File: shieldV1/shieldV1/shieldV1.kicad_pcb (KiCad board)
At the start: 2 copper layers, 70 x 59 mm, 2 parts, among them J1 Conn_02x19_Odd_Even, J2 Conn_02x19_Odd_Even

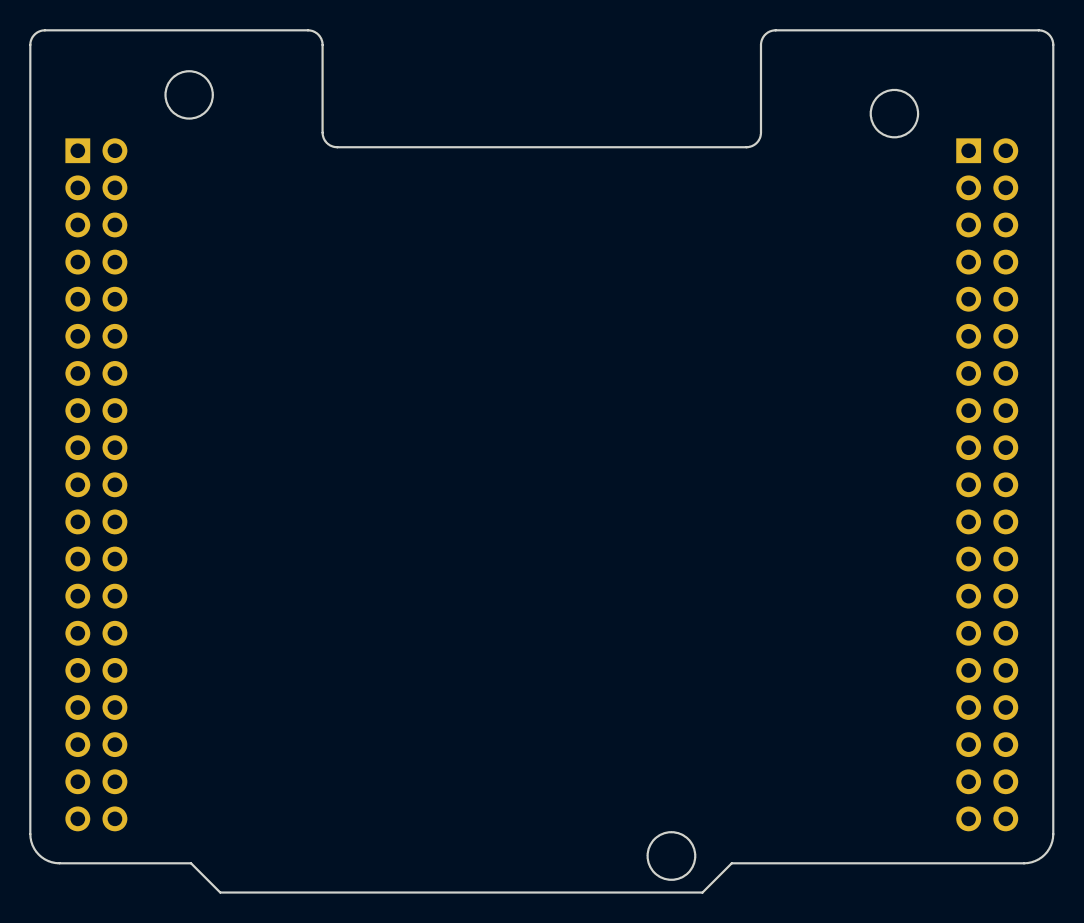
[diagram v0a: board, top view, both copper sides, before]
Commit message: Add hall sensor PCB
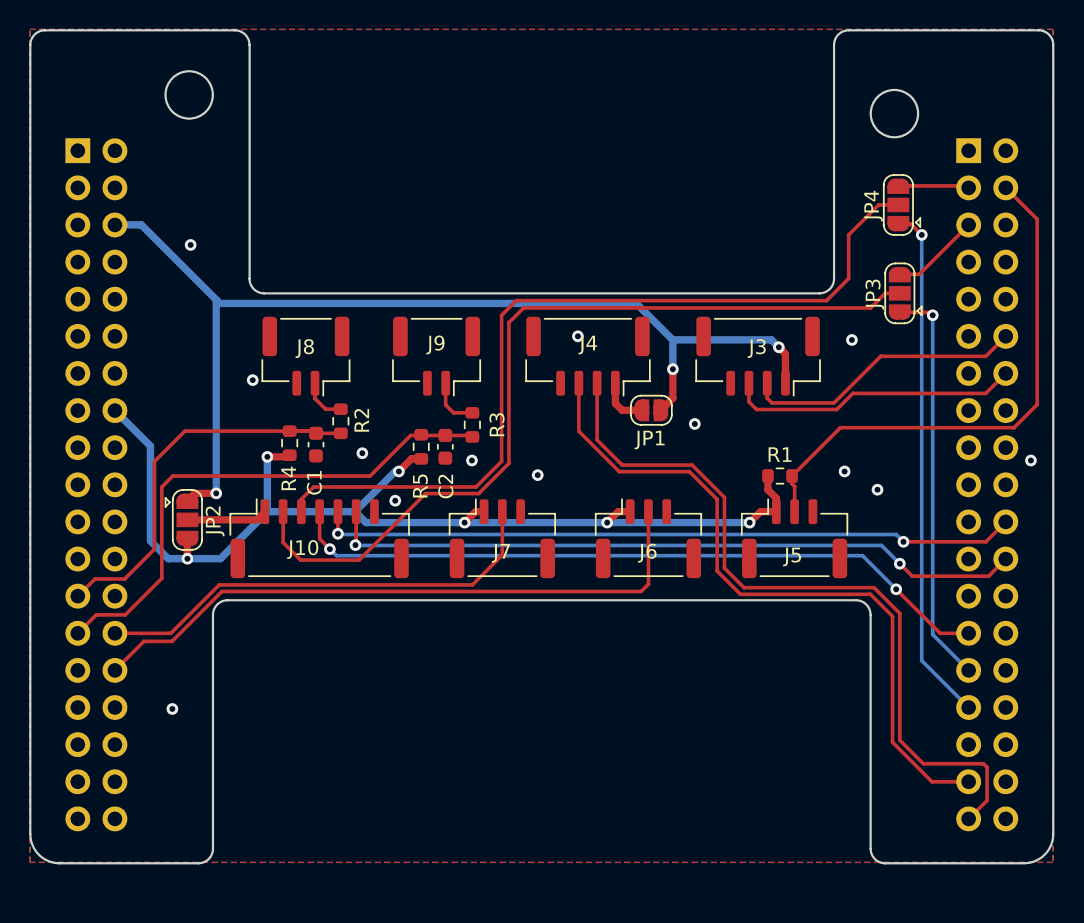
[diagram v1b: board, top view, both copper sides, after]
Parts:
- added C1: C, Capacitor_SMD:C_0603_1608Metric, F.Cu at (52.1, 121.7)
- added C2: C, Capacitor_SMD:C_0603_1608Metric, F.Cu at (60.9, 121.8)
- added J10: Conn_01x07_Female, Connector_JST:JST_GH_SM07B-GHS-TB_1x07-1MP_P1.25mm_Horizontal, F.Cu at (52.3, 128.1)
- added J3: Conn_01x04_Female, Connector_JST:JST_GH_SM04B-GHS-TB_1x04-1MP_P1.25mm_Horizontal, F.Cu at (82.3, 115.6)
- added J4: Conn_01x04_Female, Connector_JST:JST_GH_SM04B-GHS-TB_1x04-1MP_P1.25mm_Horizontal, F.Cu at (70.7, 115.6)
- added J5: Conn_01x03_Female, Connector_JST:JST_GH_SM03B-GHS-TB_1x03-1MP_P1.25mm_Horizontal, F.Cu at (84.8, 128.1)
- added J6: Conn_01x03_Female, Connector_JST:JST_GH_SM03B-GHS-TB_1x03-1MP_P1.25mm_Horizontal, F.Cu at (74.8, 128.1)
- added J7: Conn_01x03_Female, Connector_JST:JST_GH_SM03B-GHS-TB_1x03-1MP_P1.25mm_Horizontal, F.Cu at (64.8, 128.1)
- added J8: Conn_01x02_Female, Connector_JST:JST_GH_SM02B-GHS-TB_1x02-1MP_P1.25mm_Horizontal, F.Cu at (51.4, 115.6)
- added J9: Conn_01x02_Female, Connector_JST:JST_GH_SM02B-GHS-TB_1x02-1MP_P1.25mm_Horizontal, F.Cu at (60.3, 115.6)
- added JP1: SolderJumper_2_Open, Jumper:SolderJumper-2_P1.3mm_Open_RoundedPad1.0x1.5mm, F.Cu at (75.0, 119.3)
- added JP2: SolderJumper_3_Open, Jumper:SolderJumper-3_P1.3mm_Open_RoundedPad1.0x1.5mm, F.Cu at (43.3, 126.8)
- added JP3: SolderJumper_3_Open, Jumper:SolderJumper-3_P1.3mm_Open_RoundedPad1.0x1.5mm, F.Cu at (92.0, 111.3)
- added JP4: SolderJumper_3_Open, Jumper:SolderJumper-3_P1.3mm_Open_RoundedPad1.0x1.5mm, F.Cu at (91.9, 105.3)
- added R1: 10K, Resistor_SMD:R_0603_1608Metric, F.Cu at (83.8, 123.8)
- added R2: 10K, Resistor_SMD:R_0603_1608Metric, F.Cu at (53.8, 120.1)
- added R3: 10K, Resistor_SMD:R_0603_1608Metric, F.Cu at (62.8, 120.3)
- added R4: 10K, Resistor_SMD:R_0603_1608Metric, F.Cu at (50.3, 121.6)
- added R5: 10K, Resistor_SMD:R_0603_1608Metric, F.Cu at (59.3, 121.8)
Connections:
- J1 pad 16: (no net) -> +3V3
- J1 pad 19: (no net) -> GND
- J1 pad 20: (no net) -> GND
- J1 pad 22: (no net) -> GND
- J1 pad 25: (no net) -> /PC14
- J1 pad 27: (no net) -> /PC15
- J1 pad 28: (no net) -> /PA_0_ADC1_0
- J1 pad 30: (no net) -> /PA1_ADC1_1
- J1 pad 6: (no net) -> +5V
- J1 pad 8: (no net) -> GND
- J2 pad 12: (no net) -> /PA_12_UART6_RX
- J2 pad 14: (no net) -> /PA_11_UART6_TX
- J2 pad 20: (no net) -> GND
- J2 pad 22: (no net) -> /PB2
- J2 pad 24: (no net) -> /PB1
- J2 pad 27: (no net) -> /PB4_SPI1_MISO
- J2 pad 29: (no net) -> /PB5_SPI1_MOSI
- J2 pad 3: (no net) -> /PB8_I2C1_SCL
- J2 pad 31: (no net) -> /PB3_SPI1_SCLK
- J2 pad 32: (no net) -> GND
- J2 pad 35: (no net) -> /PA_2_UART2_TX
- J2 pad 37: (no net) -> /PA_3_UART2_RX
- J2 pad 4: (no net) -> /PC6_CRANK_SIG
- J2 pad 5: (no net) -> /PB9_I2C1_SDA
- J2 pad 9: (no net) -> GND
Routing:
- net +3V3: track 0.00 -> 74.1 mm, vias 0 -> 6
- net +5V: track 0.00 -> 72.1 mm, vias 0 -> 3
- net Net-(J10-Pad2): track 0.00 -> 58.0 mm
- net Net-(J10-Pad3): track 0.00 -> 57.6 mm
- net /PA_3_UART2_RX: track 0.00 -> 51.8 mm
- net /PB4_SPI1_MISO: track 0.00 -> 48.9 mm, vias 0 -> 2
- net /PB1: track 0.00 -> 48.2 mm, vias 0 -> 2
- net /PB2: track 0.00 -> 48.0 mm, vias 0 -> 2
- net /PA_2_UART2_TX: track 0.00 -> 47.8 mm
- net /PA1_ADC1_1: track 0.00 -> 43.9 mm
- net /PC6_CRANK_SIG: track 0.00 -> 37.3 mm
- net /PC15: track 0.00 -> 36.3 mm
- net /PB3_SPI1_SCLK: track 0.00 -> 35.6 mm, vias 0 -> 1
- net /PA_0_ADC1_0: track 0.00 -> 31.7 mm
- net /PC14: track 0.00 -> 27.9 mm
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- added copper zone on B.Cu, net GND
- added copper zone on F.Cu, net GND
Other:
- board size 70 x 59 mm -> 70 x 57 mm

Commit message: Add shield fab output
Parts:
- moved JP1 0.79 mm to (75.0, 120.1)
- moved JP2 0.47 mm to (43.8, 126.8)
- moved R2 0.24 mm to (53.8, 120.3)
- moved R4 0.20 mm to (50.3, 121.8)
- moved C1 0.10 mm to (52.1, 121.8)
- moved C2 0.10 mm to (60.9, 121.9)
- moved R5 0.10 mm to (59.3, 121.9)
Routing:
- net +5V: track 72.1 -> 72.6 mm
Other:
- board text added: "3V3"
- board text added: "5V"
- board text added: "CRANK"
- board text added: "LCD"
- board text added: "LCD com"
- board text added: "LCD pwr"
- board text added: "POT0"
- board text added: "POT1"
- board text added: "SW0"
- board text added: "SW1"
- board text added: "V1.1 Coilchain 11.02.2021"
- board text added: "VESC0"
- board text added: "VESC1"
- board text added: "i2c"
- board text added: "spi"
